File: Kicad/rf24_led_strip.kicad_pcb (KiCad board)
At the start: 2 copper layers, 23.6 x 28.2 mm, 27 parts, among them IC1 ATMEGA328-P, P1 UART, P2 12V in, P3 LED_OUT, Q1 Q_NMOS_GDS, Q2 Q_NMOS_GDS, Q3 Q_NMOS_GDS, U1 LM_1117, U2 LM_1117, U3 nrf24l01+

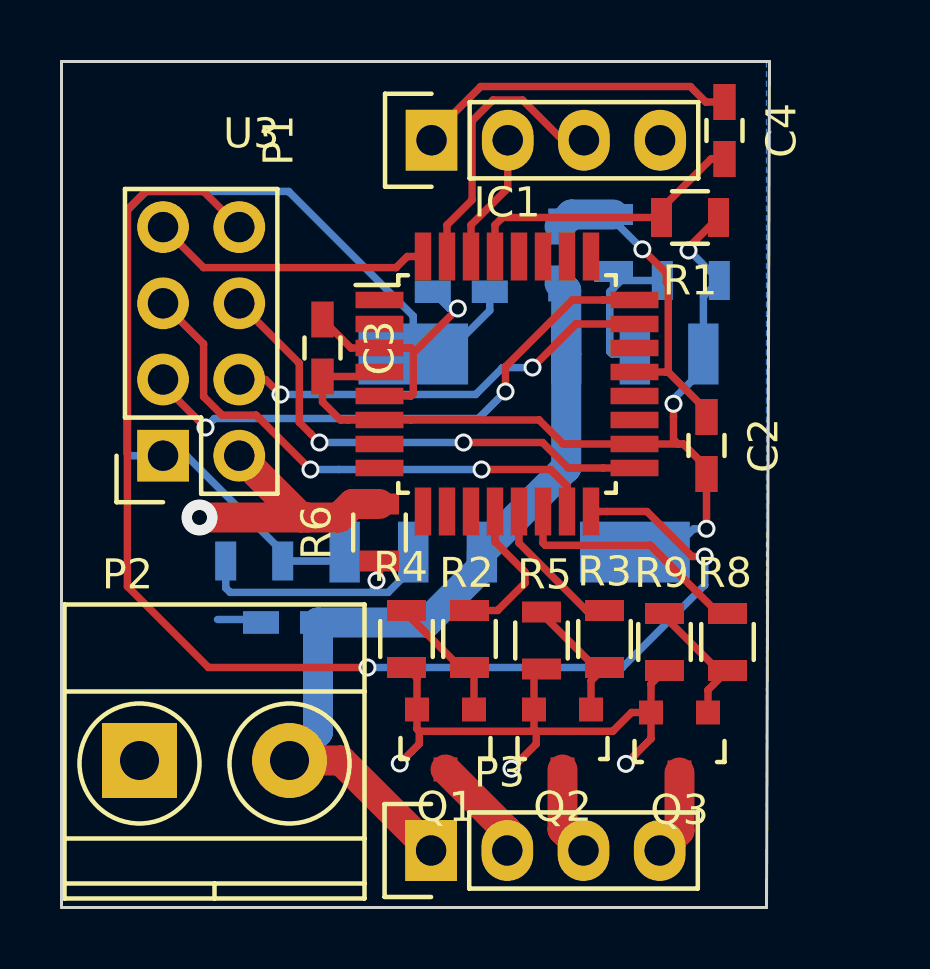
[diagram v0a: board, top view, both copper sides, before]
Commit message: 3.3V Version.
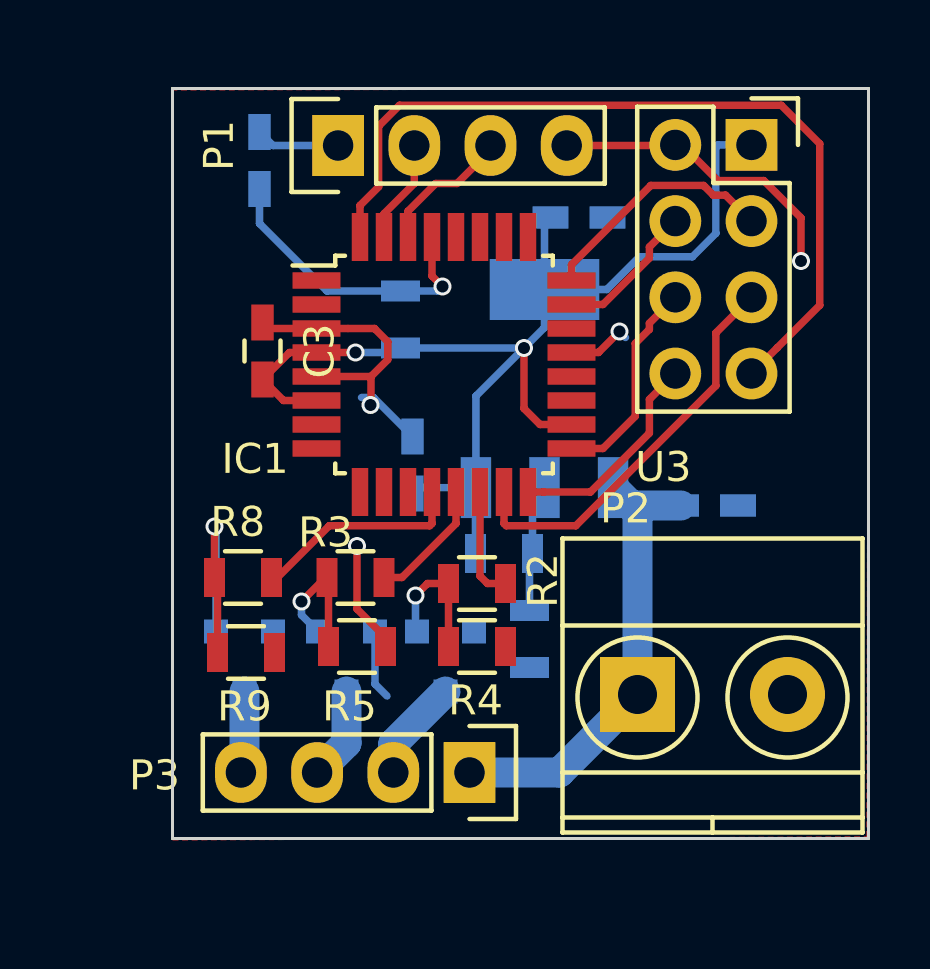
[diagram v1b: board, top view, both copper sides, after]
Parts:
- removed C2: C, Capacitors_SMD:C_0603_HandSoldering
- removed R10, R11: R, Resistors_SMD:R_0805
- removed U1: LM_1117, TO_SOT_Packages_SMD:SOT-223
- C4, Q1, Q2, Q3, R1, R6: moved to B.Cu
- moved U3 22.2 mm to (122.3, 100.9), turned to 270 degrees
- moved P2 16.7 mm to (118.5, 119.2)
- moved R8 16.3 mm to (105.3, 115.3), turned to 0 degrees
- moved C4 15.5 mm to (105.9, 101.4)
- moved Q3 14.7 mm to (105.4, 118.1), turned to 0 degrees
- moved C7 14.5 mm to (120.9, 112.9), turned to 180 degrees
- moved R9 14.0 mm to (105.5, 117.8), turned to 180 degrees
- moved R1 10.2 mm to (110.6, 106.7), turned to 90 degrees
- moved R3 8.55 mm to (109.1, 115.3), turned to 0 degrees
- moved R7 8.33 mm to (114.0, 114.5), turned to 180 degrees
- moved Q2 7.65 mm to (108.8, 118.1), turned to 0 degrees
- moved R5 6.15 mm to (109.2, 117.6), turned to 180 degrees
- moved R6 6.13 mm to (114.9, 117.3), turned to 270 degrees
- moved C8 6.00 mm to (111.0, 111.5), turned to 270 degrees
- moved U2 4.87 mm to (115.4, 109.0)
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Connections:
- C1 pad 1: GND -> +3V3
- C1 pad 2: +12V -> GND
- C3 pad 2: +5V -> +3V3
- IC1 pad 12: /RED_PWM -> /BLUE_PWM
- IC1 pad 14: /BLUE_PWM -> /RED_PWM
- IC1 pad 18: +5V -> +3V3
- IC1 pad 4: +5V -> +3V3
- IC1 pad 6: +5V -> +3V3
- P1 pad 2: /RX -> /TX
- P1 pad 3: /TX -> /RX
- P2 pad 1: GND -> +12V
- P2 pad 2: +12V -> GND
- R1 pad 1: +5V -> +3V3
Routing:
- net /MISO: track 43.9 -> 7.25 mm, vias 2 -> 0
- net +5V: track 30.8 -> 0.00 mm, vias 3 -> 0
- net GND: track 50.4 -> 29.3 mm, vias 6 -> 4
- net /IRQ: track 9.38 -> 28.1 mm
- net +12V: track 28.0 -> 16.4 mm
- net /CSN: track 18.7 -> 8.11 mm, vias 2 -> 0
- net /CE: track 14.4 -> 4.83 mm, vias 2 -> 0
- net /SCK: track 16.6 -> 7.09 mm, vias 2 -> 0
- net /DTR: track 10.8 -> 2.81 mm
- net /TX: track 9.44 -> 3.47 mm
- net +3V3: track 34.5 -> 40.1 mm, vias 0 -> 2
- net Net-(R6-Pad1): track 9.70 -> 4.30 mm, vias 1 -> 0
- net Net-(R10-Pad1): track 5.32 -> 0.00 mm
- net /MOSI: track 17.9 -> 13.5 mm, vias 2 -> 0
- net Net-(Q3-Pad1): track 4.61 -> 7.86 mm, vias 0 -> 1
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- added copper zone on F.Cu, net GND
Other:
- board size 23.6 x 28.2 mm -> 23.2 x 25 mm

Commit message: Update
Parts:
- added C10: 10µF, Capacitors_SMD:C_0805, F.Cu at (144.8, 62.2)
- added C11: 100µF, Capacitors_ThroughHole:CP_Radial_D6.3mm_P2.50mm, F.Cu at (139.0, 57.8)
- added C2: C, Capacitors_ThroughHole:C_Disc_D3.0mm_W2.0mm_P2.50mm, F.Cu at (110.2, 71.5)
- added C5: C, Capacitors_ThroughHole:C_Disc_D3.0mm_W2.0mm_P2.50mm, F.Cu at (110.2, 77.2)
- added C6: C, Capacitors_SMD:C_0603_HandSoldering, F.Cu at (114.8, 65.8)
- added C9: C, Capacitors_SMD:C_0603_HandSoldering, F.Cu at (102.2, 68.3)
- added JP1: 5V, Connect:GS2, F.Cu at (103.0, 87.1)
- added JP2: 12V, Connect:GS2, F.Cu at (107.0, 87.1)
- added P4: LED3_OUT, Pin_Headers:Pin_Header_Straight_1x04_Pitch2.54mm, F.Cu at (135.2, 95.0)
- added P5: LED2_OUT, Pin_Headers:Pin_Header_Straight_1x04_Pitch2.54mm, F.Cu at (147.6, 95.0)
- added P6: WS2812, Pin_Headers:Pin_Header_Straight_1x03_Pitch2.54mm, F.Cu at (102.7, 73.5)
- added Q4: Q_NMOS_GDS, TO_SOT_Packages_SMD:SOT-23, B.Cu at (138.7, 91.3)
- added Q5: Q_NMOS_GDS, TO_SOT_Packages_SMD:SOT-23, B.Cu at (146.0, 91.3)
- added Q6: Q_NMOS_GDS, TO_SOT_Packages_SMD:SOT-23, B.Cu at (142.3, 91.3)
- added Q7: Q_NMOS_GDS, TO_SOT_Packages_SMD:SOT-23, B.Cu at (126.3, 91.2)
- added Q8: Q_NMOS_GDS, TO_SOT_Packages_SMD:SOT-23, B.Cu at (133.8, 91.2)
- added Q9: Q_NMOS_GDS, TO_SOT_Packages_SMD:SOT-23, B.Cu at (130.2, 91.2)
- added R10: R, Resistors_SMD:R_0805, F.Cu at (140.0, 81.4)
- added R11: R, Resistors_SMD:R_0805, F.Cu at (147.0, 81.4)
- added R12: R, Resistors_SMD:R_0805, F.Cu at (143.5, 81.4)
- added R13: R, Resistors_SMD:R_0805, B.Cu at (138.6, 86.9)
- added R14: R, Resistors_SMD:R_0805, B.Cu at (146.1, 86.8)
- added R15: R, Resistors_SMD:R_0805, B.Cu at (142.3, 86.8)
- added R16: R, Resistors_SMD:R_0805, F.Cu at (129.5, 81.4)
- added R17: R, Resistors_SMD:R_0805, F.Cu at (136.5, 81.4)
- added R18: R, Resistors_SMD:R_0805, F.Cu at (133.0, 81.4)
- added R19: R, Resistors_SMD:R_0805, B.Cu at (126.2, 86.4)
- added R20: R, Resistors_SMD:R_0805, B.Cu at (133.7, 86.4)
- added R21: R, Resistors_SMD:R_0805, B.Cu at (129.9, 86.4)
- added R22: R, Resistors_SMD:R_0805, F.Cu at (106.0, 69.8)
- added R23: R, Resistors_SMD:R_0805, F.Cu at (106.3, 66.2)
- added R24: R, Resistors_SMD:R_0805, F.Cu at (121.2, 65.5)
- added R25: R, Resistors_SMD:R_0805, F.Cu at (107.5, 36.0)
- added R26: R, Resistors_SMD:R_0805, F.Cu at (112.5, 43.2)
- added R27: R, Resistors_SMD:R_0805, F.Cu at (109.7, 42.0)
- added REF**: MountingHole_3.2mm_M3, Mounting_Holes:MountingHole_3.2mm_M3, F.Cu at (103.5, 53.5)
- added REF**: MountingHole_3.2mm_M3, Mounting_Holes:MountingHole_3.2mm_M3, F.Cu at (146.4, 53.5)
- added REF***: OSHW-Logo2_7.3x6mm_SilkScreen, Symbols:OSHW-Logo2_7.3x6mm_SilkScreen, F.Cu at (111.5, 53.8)
- added REF***: KiCad-Logo2_8mm_SilkScreen, Symbols:KiCad-Logo2_8mm_SilkScreen, F.Cu at (108.8, 61.0)
- added U1: LM_1117, TO_SOT_Packages_SMD:SOT-223, F.Cu at (112.8, 84.2)
- added U4: ESP-01, Pin_Headers:Pin_Header_Straight_2x04_Pitch2.54mm, F.Cu at (127.2, 55.3)
- added Y1: Crystal, Crystals:Crystal_HC49-4H_Vertical, F.Cu at (114.5, 71.0)
- C1: value C -> 100nF; moved to F.Cu
- C4, C7, C8, R1, R6, R7, U2: moved to F.Cu
- P1, P3: footprint Pin_Headers:Pin_Header_Straight_1x04 -> Pin_Headers:Pin_Header_Straight_1x04_Pitch2.54mm
- R4, R5, R9: moved to B.Cu
- U3: footprint Socket_Strips:Socket_Strip_Straight_2x04 -> Pin_Headers:Pin_Header_Straight_2x04_Pitch2.54mm
- moved C4 60.6 mm to (116.2, 41.7), turned to 90 degrees
- moved C8 56.6 mm to (139.3, 62.5), turned to 0 degrees
- moved P1 54.9 mm to (121.2, 47.5), turned to 270 degrees
- moved R6 51.8 mm to (138.1, 71.0), turned to 0 degrees
- moved U2 48.6 mm to (133.1, 63.8), turned to 0 degrees
- moved C7 48.4 mm to (139.0, 68.0), turned to 90 degrees
- moved C1 48.4 mm to (144.8, 64.0)
- moved R7 48.1 mm to (134.5, 71.0)
- moved R1 43.9 mm to (123.8, 64.8), turned to 270 degrees
- moved U3 40.5 mm to (143.5, 66.4), turned to 0 degrees
- moved C3 38.5 mm to (118.2, 71.2)
- moved IC1 38.4 mm to (124.2, 71.8)
- moved R8 36.5 mm to (119.0, 81.4), turned to 90 degrees
- moved R3 36.5 mm to (122.5, 81.4), turned to 90 degrees
- moved R2 36.4 mm to (126.0, 81.4), turned to 90 degrees
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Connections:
- net +12V renamed VCC
- C3 pad 2: +3V3 -> +5V
- IC1 pad 1: (no net) -> /CE
- IC1 pad 10: (no net) -> Net-(IC1-Pad10)
- IC1 pad 11: (no net) -> Net-(IC1-Pad11)
- IC1 pad 18: +3V3 -> +5V
- IC1 pad 2: (no net) -> /CSN
- IC1 pad 23: /CE -> /GREEN2_PWM
- IC1 pad 24: /CSN -> /RED2_PWM
- IC1 pad 25: (no net) -> /BLUE2_PWM
- IC1 pad 26: (no net) -> /RED3_PWM
- IC1 pad 27: (no net) -> /GREEN3_PWM
- IC1 pad 28: (no net) -> /BLUE3_PWM
- IC1 pad 4: +3V3 -> +5V
- IC1 pad 6: +3V3 -> +5V
- IC1 pad 7: (no net) -> Net-(C2-Pad1)
- IC1 pad 8: (no net) -> Net-(C5-Pad1)
- IC1 pad 9: (no net) -> Net-(IC1-Pad9)
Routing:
- net +3V3: track 40.1 -> 2.54 mm, vias 2 -> 0
- net VCC: track 16.4 -> 53.7 mm
- net GND: track 29.3 -> 0.00 mm, vias 4 -> 0
- net /IRQ: track 28.1 -> 0.00 mm
- net /RED2_PWM: track 0.00 -> 23.3 mm, vias 0 -> 2
- net /CE: track 4.83 -> 27.0 mm, vias 0 -> 2
- net /BLUE2_PWM: track 0.00 -> 22.1 mm, vias 0 -> 2
- net /GREEN2_PWM: track 0.00 -> 19.8 mm, vias 0 -> 2
- net /RED3_PWM: track 0.00 -> 19.1 mm, vias 0 -> 2
- net /GREEN3_PWM: track 0.00 -> 16.6 mm, vias 0 -> 2
- net /CSN: track 8.11 -> 23.8 mm, vias 0 -> 2
- net /MOSI: track 13.5 -> 28.9 mm
- net /BLUE3_PWM: track 0.00 -> 15.1 mm, vias 0 -> 2
- net +5V: track 0.00 -> 14.7 mm
- net /SCK: track 7.09 -> 19.8 mm
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- removed copper zone on B.Cu, net GND
- removed copper zone on F.Cu, net GND
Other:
- board size 23.2 x 25 mm -> 50 x 50 mm
- net class Dick added: clearance 0.3, trace_width 0.5, via_dia 0.6, via_drill 0.4
- net class Power: via_dia 0.6 -> 0.8; via_drill 0.4 -> 0.6
- rule pad_to_mask_clearance: 0 -> 0.05
- board text added: "12V"
- board text added: "5V"

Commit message: STM32 schematic done.
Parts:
- removed C3: C, Capacitors_SMD:C_0603_HandSoldering
- removed IC1: ATMEGA328-P, Housings_QFP:TQFP-32_7x7mm_Pitch0.8mm
- removed Q1: Q_NMOS_GDS, TO_SOT_Packages_SMD:SOT-23
- removed R1, R2: R, Resistors_SMD:R_0805
- removed REF** (x2): MountingHole_3.2mm_M3, Mounting_Holes:MountingHole_3.2mm_M3
- removed REF***: OSHW-Logo2_7.3x6mm_SilkScreen, Symbols:OSHW-Logo2_7.3x6mm_SilkScreen
- removed REF***: KiCad-Logo2_8mm_SilkScreen, Symbols:KiCad-Logo2_8mm_SilkScreen
- added C12: 100nF, Capacitors_SMD:C_0603_HandSoldering, F.Cu at (125.0, 79.8)
- added C13: 100nF, Capacitors_SMD:C_0603_HandSoldering, F.Cu at (128.2, 71.3)
- added C14: 100nF, Capacitors_SMD:C_0603_HandSoldering, F.Cu at (119.5, 67.8)
- added D1: D, Diodes_ThroughHole:D_DO-15_P12.70mm_Horizontal, B.Cu at (147.8, 73.0)
- added P11: CONN_01X07, Pin_Headers:Pin_Header_Straight_1x07_Pitch2.54mm, F.Cu at (101.8, 67.5)
- added P7: USB_OTG, Connect:USB_Micro-B, F.Cu at (147.7, 66.2)
- added P8: SWD, Pin_Headers:Pin_Header_Straight_1x05_Pitch2.54mm, F.Cu at (131.2, 68.2)
- added P9: UART, Pin_Headers:Pin_Header_Straight_1x03_Pitch2.54mm, F.Cu at (112.5, 80.5)
- added Q10: Q_NMOS_GDS, TO_SOT_Packages_SMD:SOT-23, B.Cu at (140.8, 76.8)
- added Q11: Q_NMOS_GDS, TO_SOT_Packages_SMD:SOT-23, B.Cu at (129.0, 57.2)
- added Q12: Q_NMOS_GDS, TO_SOT_Packages_SMD:SOT-23, B.Cu at (121.5, 57.2)
- added Q13: Q_NMOS_GDS, TO_SOT_Packages_SMD:SOT-23, B.Cu at (136.5, 57.2)
- added Q14: Q_NMOS_GDS, TO_SOT_Packages_SMD:SOT-23, B.Cu at (140.0, 57.2)
- added Q15: Q_NMOS_GDS, TO_SOT_Packages_SMD:SOT-23, B.Cu at (132.8, 57.2)
- added Q16: Q_NMOS_GDS, TO_SOT_Packages_SMD:SOT-23, B.Cu at (125.2, 57.2)
- added R28: R, Resistors_SMD:R_0805, F.Cu at (136.7, 60.0)
- added R29: R, Resistors_SMD:R_0805, F.Cu at (139.8, 62.3)
- added R30: R, Resistors_SMD:R_0805, F.Cu at (133.0, 62.2)
- added R31: R, Resistors_SMD:R_0805, F.Cu at (125.5, 62.3)
- added R32: R, Resistors_SMD:R_0805, F.Cu at (140.2, 59.8)
- added R33: R, Resistors_SMD:R_0805, F.Cu at (132.8, 60.0)
- added R34: R, Resistors_SMD:R_0805, F.Cu at (125.2, 59.8)
- added R35: R, Resistors_SMD:R_0805, F.Cu at (141.1, 65.2)
- added R36: R, Resistors_SMD:R_0805, F.Cu at (141.1, 67.2)
- added R37: R, Resistors_SMD:R_0805, F.Cu at (141.1, 69.2)
- added R38: R, Resistors_SMD:R_0805, F.Cu at (116.8, 58.0)
- added R39: R, Resistors_SMD:R_0805, F.Cu at (110.2, 53.0)
- added R40: R, Resistors_SMD:R_0805, F.Cu at (118.8, 60.5)
- added R41: R, Resistors_SMD:R_0805, F.Cu at (120.5, 84.7)
- C11: value 100µF -> 100nF; footprint Capacitors_ThroughHole:CP_Radial_D6.3mm_P2.50mm -> Capacitors_SMD:C_0603_HandSoldering
- C2: value C -> 10µF; footprint Capacitors_ThroughHole:C_Disc_D3.0mm_W2.0mm_P2.50mm -> Capacitors_SMD:C_0805
- C4: footprint Capacitors_SMD:C_0603_HandSoldering -> Capacitors_ThroughHole:C_Disc_D3.0mm_W2.0mm_P2.50mm
- C6, C9: value C -> 100nF
- JP1: value 5V -> Jumper; footprint Connect:GS2 -> Pin_Headers:Pin_Header_Straight_1x02_Pitch2.54mm
- JP2: value 12V -> Jumper; footprint Connect:GS2 -> Pin_Headers:Pin_Header_Straight_1x02_Pitch2.54mm
- P1: value UART -> 12V in; footprint Pin_Headers:Pin_Header_Straight_1x04_Pitch2.54mm -> Terminal_Blocks:TerminalBlock_Pheonix_MKDS1.5-2pol
- P2: value 12V in -> LED_OUT; footprint Terminal_Blocks:TerminalBlock_Pheonix_MKDS1.5-2pol -> Pin_Headers:Pin_Header_Straight_1x04_Pitch2.54mm
- P3: value LED_OUT -> LED2_OUT
- P5: value LED2_OUT -> LED4_OUT
- P6: value WS2812 -> LED5_OUT; footprint Pin_Headers:Pin_Header_Straight_1x03_Pitch2.54mm -> Pin_Headers:Pin_Header_Straight_1x04_Pitch2.54mm
- R13, R14, R15, R19, R20, R21, R4, R5, R9: moved to F.Cu
- U1: value LM_1117 -> nrf24l01+; footprint TO_SOT_Packages_SMD:SOT-223 -> Pin_Headers:Pin_Header_Straight_2x04_Pitch2.54mm
- U2: value LM_1117 -> ESP-01; footprint TO_SOT_Packages_SMD:SOT-223 -> Pin_Headers:Pin_Header_Straight_2x04_Pitch2.54mm
- U3: value nrf24l01+ -> STM32F103C8Tx; footprint Pin_Headers:Pin_Header_Straight_2x04_Pitch2.54mm -> Housings_QFP:LQFP-48_7x7mm_Pitch0.5mm
- U4: value ESP-01 -> LM_1117; footprint Pin_Headers:Pin_Header_Straight_2x04_Pitch2.54mm -> TO_SOT_Packages_SMD:SOT-223
- moved P1 50.8 mm to (145.2, 92.2), turned to 90 degrees
- moved C1 44.0 mm to (103.0, 78.0)
- moved P5 41.8 mm to (140.8, 53.8)
- moved R25 39.7 mm to (137.0, 62.5), turned to 270 degrees
- moved U2 36.9 mm to (114.8, 95.8), turned to 270 degrees
- moved P6 33.1 mm to (129.3, 53.8), turned to 270 degrees
- moved C8 32.9 mm to (107.0, 56.2), turned to 90 degrees
- moved R22 32.7 mm to (138.0, 76.8), turned to 270 degrees
- moved R15 29.4 mm to (113.5, 93.0), turned to 0 degrees
- moved C11 29.0 mm to (116.0, 75.5), turned to 270 degrees
- moved JP1 28.6 mm to (118.8, 63.2), turned to 270 degrees
- moved C4 26.4 mm to (106.5, 66.2), turned to 180 degrees
- moved R6 25.9 mm to (119.0, 88.5), turned to 180 degrees
- moved C7 25.7 mm to (116.7, 55.2), turned to 180 degrees
- moved C10 25.6 mm to (119.5, 66.2), turned to 180 degrees
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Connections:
- C10 pad 1: +3V3 -> GND
- C10 pad 2: GND -> +3V3
- C11 pad 1: +3V3 -> GND
- C11 pad 2: GND -> +3V3
- C2 pad 1: Net-(C2-Pad1) -> +3V3
- C4 pad 1: /DTR -> Net-(C4-Pad1)
- C4 pad 2: Net-(C4-Pad2) -> GND
- C6 pad 1: GND -> /NRST
- C6 pad 2: +12V -> GND
- C7 pad 2: VCC -> +12V
- C9 pad 1: GND -> +3V3
- C9 pad 2: +5V -> GND
- JP1 pad 1: VCC -> /BOOT0
- JP1 pad 2: +5V -> +3V3
- JP2 pad 1: VCC -> /BOOT1
- JP2 pad 2: +12V -> +3V3
- P1 pad 1: /DTR -> GND
- P1 pad 2: /TX -> +12V
- P2 pad 1: VCC -> +12V
- P2 pad 2: GND -> /RED
- P3 pad 1: VCC -> +12V
- P3 pad 2: /RED -> /RED2
- P3 pad 3: /GREEN -> /GREEN2
- P3 pad 4: /BLUE -> /BLUE2
- P4 pad 1: VCC -> +12V
- P5 pad 1: VCC -> +12V
- P5 pad 2: /RED2 -> /RED5
- P5 pad 3: /GREEN2 -> /GREEN5
- P5 pad 4: /BLUE2 -> /BLUE5
- P6 pad 1: Net-(IC1-Pad9) -> +12V
- P6 pad 2: Net-(IC1-Pad10) -> /RED4
- P6 pad 3: Net-(IC1-Pad11) -> /GREEN4
- Q2 pad 3: /GREEN -> /RED
- Q4 pad 3: /BLUE2 -> /GREEN
- Q6 pad 3: /GREEN2 -> /BLUE2
- Q7 pad 3: /BLUE3 -> /GREEN2
- Q9 pad 3: /GREEN3 -> /BLUE3
- R10 pad 1: Net-(Q4-Pad1) -> Net-(Q6-Pad1)
- R11 pad 1: Net-(Q5-Pad1) -> Net-(Q7-Pad1)
- R11 pad 2: /RED2_PWM -> /GREEN2_PWM
- R12 pad 1: Net-(Q6-Pad1) -> GND
- R12 pad 2: /GREEN2_PWM -> Net-(Q5-Pad1)
- R13 pad 2: Net-(Q4-Pad1) -> Net-(Q6-Pad1)
- R14 pad 2: Net-(Q5-Pad1) -> Net-(Q7-Pad1)
- R15 pad 1: GND -> Net-(R15-Pad1)
- R15 pad 2: Net-(Q6-Pad1) -> +3V3
- R16 pad 1: Net-(Q7-Pad1) -> Net-(R16-Pad1)
- R16 pad 2: /BLUE3_PWM -> +3V3
- R18 pad 2: /GREEN3_PWM -> /BLUE3_PWM
- R19 pad 1: GND -> Net-(Q10-Pad1)
- R19 pad 2: Net-(Q7-Pad1) -> /GREEN3_PWM
- R22 pad 1: Net-(R22-Pad1) -> GND
- R22 pad 2: GND -> Net-(Q10-Pad1)
- R23 pad 1: Net-(R22-Pad1) -> Net-(Q11-Pad1)
- R23 pad 2: +5V -> /RED4_PWM
- R24 pad 1: Net-(R24-Pad1) -> Net-(Q12-Pad1)
- R24 pad 2: /TX -> /BLUE4_PWM
- R25 pad 1: GND -> Net-(Q13-Pad1)
- R25 pad 2: Net-(R24-Pad1) -> /GREEN4_PWM
- R26 pad 1: Net-(R26-Pad1) -> GND
- R26 pad 2: +3V3 -> Net-(Q11-Pad1)
- R27 pad 1: Net-(R27-Pad1) -> GND
- R27 pad 2: +3V3 -> Net-(Q12-Pad1)
- R3 pad 2: /GREEN_PWM -> /RED_PWM
- R4 pad 1: GND -> Net-(Q3-Pad1)
- R4 pad 2: Net-(Q1-Pad1) -> /BLUE_PWM
- R5 pad 1: GND -> Net-(Q4-Pad1)
- R5 pad 2: Net-(Q2-Pad1) -> /GREEN_PWM
- R6 pad 1: Net-(R6-Pad1) -> GND
- R6 pad 2: GND -> Net-(Q2-Pad1)
- R7 pad 1: Net-(R6-Pad1) -> GND
- R7 pad 2: +3V3 -> Net-(Q3-Pad1)
- R8 pad 1: Net-(Q3-Pad1) -> GND
- R8 pad 2: /BLUE_PWM -> Net-(Q4-Pad1)
- R9 pad 1: GND -> Net-(Q5-Pad1)
- R9 pad 2: Net-(Q3-Pad1) -> /RED2_PWM
- U1 pad 1: +12V -> +3V3
- U1 pad 2: Net-(R22-Pad1) -> GND
- U1 pad 3: +5V -> /CSN
- U1 pad 4: +5V -> /CE
- U2 pad 1: VCC -> +3V3
- U2 pad 2: Net-(R6-Pad1) -> /TX
- U2 pad 3: +3V3 -> Net-(R15-Pad1)
- U2 pad 4: +3V3 -> (no net)
- U3 pad 2: GND -> /CSN
- U3 pad 3: /CSN -> /CE
- U3 pad 4: /CE -> /IRQ
- U3 pad 5: /MOSI -> Net-(C4-Pad1)
- U3 pad 6: /SCK -> Net-(C5-Pad1)
- U3 pad 7: /IRQ -> /NRST
- U3 pad 8: /MISO -> GND
- U4 pad 1: +3V3 -> +12V
- U4 pad 2: Net-(R24-Pad1) -> Net-(R38-Pad1)
- U4 pad 3: Net-(R26-Pad1) -> +3V3
- U4 pad 4: (no net) -> +3V3
- Y1 pad 1: Net-(C2-Pad1) -> Net-(C4-Pad1)
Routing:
- net VCC: track 53.7 -> 0.00 mm
- net (no net): track 0.72 -> 44.2 mm
- net /MOSI: track 28.9 -> 0.00 mm
- net /CE: track 27.0 -> 0.00 mm, vias 2 -> 0
- net /CSN: track 23.8 -> 0.00 mm, vias 2 -> 0
- net /MISO: track 19.8 -> 0.00 mm
- net /SCK: track 19.8 -> 0.00 mm
- net +5V: track 14.7 -> 0.00 mm
- net /RED2_PWM: track 23.3 -> 11.6 mm, vias 2 -> 0
- net Net-(C2-Pad1): track 11.1 -> 0.00 mm
- net Net-(C5-Pad1): track 10.9 -> 0.00 mm
- net /RED3_PWM: track 19.1 -> 12.6 mm, vias 2 -> 0
- net +3V3: track 2.54 -> 7.93 mm
- net /GREEN2_PWM: track 19.8 -> 14.5 mm, vias 2 -> 0
- net /BLUE2_PWM: track 22.1 -> 17.4 mm, vias 2 -> 0
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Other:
- board text removed: "12V"
- board text removed: "5V"

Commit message: First pcb version.
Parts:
- moved R35 13.8 mm to (133.4, 76.8)
- moved R25 12.3 mm to (125.2, 59.0)
- moved R28 12.0 mm to (125.2, 56.5)
- moved R34 11.8 mm to (136.6, 56.5)
- moved R31 11.5 mm to (136.5, 59.0), turned to 270 degrees
- moved Q16 11.4 mm to (136.6, 57.2)
- moved Q13 11.2 mm to (125.2, 57.2)
- moved R37 6.57 mm to (135.2, 66.2)
- moved R36 5.93 mm to (135.2, 68.2)
- moved P8 4.50 mm to (131.2, 63.7)
- moved R3 3.78 mm to (119.0, 89.8)
- moved R6 3.76 mm to (119.3, 92.2)
- moved R9 3.68 mm to (130.5, 89.8)
- moved R23 3.64 mm to (129.0, 59.0)
- moved R5 3.61 mm to (122.8, 89.8)
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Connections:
- P1 pad 1: GND -> +12V
- P1 pad 2: +12V -> GND
- P8 pad 5: /NRST -> +3V3
- Q13 pad 3: /GREEN5 -> /GREEN4
- Q16 pad 3: /GREEN4 -> /GREEN5
- U3 pad 40: /RED4_PWM -> /RED5_PWM
- U3 pad 41: /GREEN4_PWM -> /GREEN5_PWM
- U3 pad 42: /BLUE4_PWM -> /BLUE5_PWM
- U3 pad 43: /RED5_PWM -> /RED4_PWM
- U3 pad 45: /GREEN5_PWM -> /GREEN4_PWM
- U3 pad 46: /BLUE5_PWM -> /BLUE4_PWM
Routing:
- net +12V: track 0.00 -> 125.1 mm
- net +3V3: track 7.93 -> 127.6 mm, vias 0 -> 4
- net GND: track 0.00 -> 71.3 mm, vias 0 -> 25
- net (no net): track 44.2 -> 0.00 mm
- net /TX: track 0.00 -> 34.3 mm, vias 0 -> 1
- net /RX: track 0.00 -> 32.6 mm, vias 0 -> 1
- net /IRQ: track 0.00 -> 30.3 mm, vias 0 -> 2
- net /CSN: track 0.00 -> 26.4 mm, vias 0 -> 1
- net /MISO: track 0.00 -> 24.9 mm, vias 0 -> 1
- net /MOSI: track 0.00 -> 24.6 mm, vias 0 -> 1
- net /SCK: track 0.00 -> 23.8 mm, vias 0 -> 1
- net /CE: track 0.00 -> 23.7 mm, vias 0 -> 1
- net /RED5_PWM: track 0.00 -> 21.5 mm
- net /NRST: track 2.16 -> 21.3 mm, vias 0 -> 1
- net Net-(P7-Pad2): track 0.00 -> 18.8 mm, vias 0 -> 2
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- added copper zone on B.Cu, net GND
